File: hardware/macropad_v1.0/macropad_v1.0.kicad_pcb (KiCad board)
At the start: 2 copper layers, 61.9 x 76.2 mm, 50 parts, among them J1 USB_C_Receptacle_USB2.0_14P, SW1 SW_Push, SW2 Rotary Encoder, SW3 Rotary Encoder, U1 USBLC6-2SC6, U2 STM32F072C8T6, U3 XC6206PxxxMR

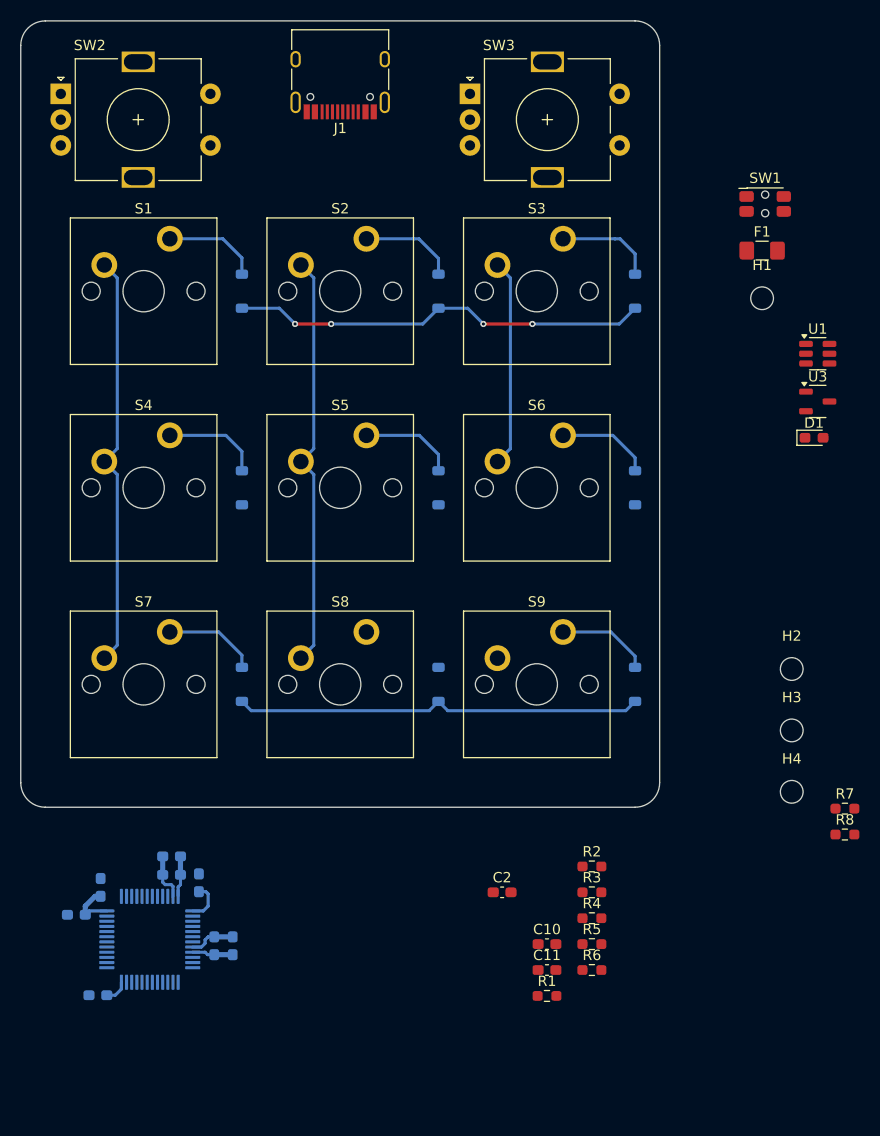
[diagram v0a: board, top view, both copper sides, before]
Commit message: finished routing decoupling caps & usb-c module
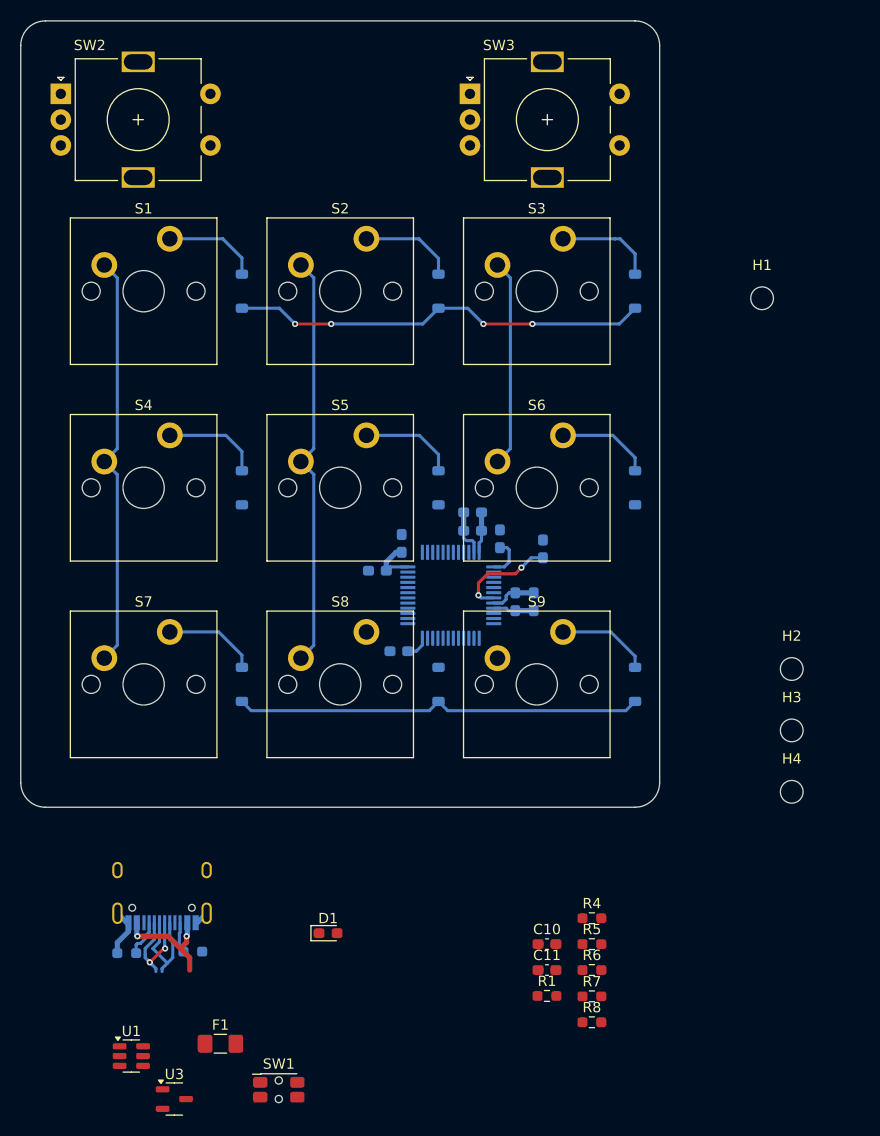
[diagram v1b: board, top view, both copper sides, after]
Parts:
- C2, J1, R2, R3: moved to B.Cu
- moved SW1 97.9 mm to (79.8, 125.0)
- moved U1 95.2 mm to (65.5, 121.7)
- moved F1 93.1 mm to (74.1, 120.6)
- moved U3 92.0 mm to (69.7, 125.9)
- moved J1 80.5 mm to (68.5, 104.8), turned to 0 degrees
- moved D1 67.2 mm to (84.6, 109.8)
- moved R2 45.9 mm to (65.0, 111.8), turned to 180 degrees
- moved C3 44.3 mm to (91.7, 72.1)
- moved C5 44.3 mm to (91.4, 82.5)
- moved C6 44.3 mm to (98.6, 70.8)
- moved C7 44.3 mm to (98.6, 69.1)
- moved C8 44.3 mm to (102.7, 77.7)
- moved C9 44.3 mm to (104.5, 77.7)
- moved U2 44.3 mm to (96.4, 77.1)
- moved C4 44.3 mm to (89.3, 74.7)
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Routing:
- net VBUS: track 0.00 -> 11.2 mm, vias 0 -> 2
- net ESD_D-: track 0.00 -> 10.1 mm, vias 0 -> 2
- net ESD_D+: track 0.00 -> 10.1 mm
- net /NRST: track 0.00 -> 10.0 mm, vias 0 -> 2
- net GND: track 9.12 -> 15.4 mm
- net Net-(J1-CC1): track 0.00 -> 3.64 mm
- net Net-(J1-CC2): track 0.00 -> 2.99 mm

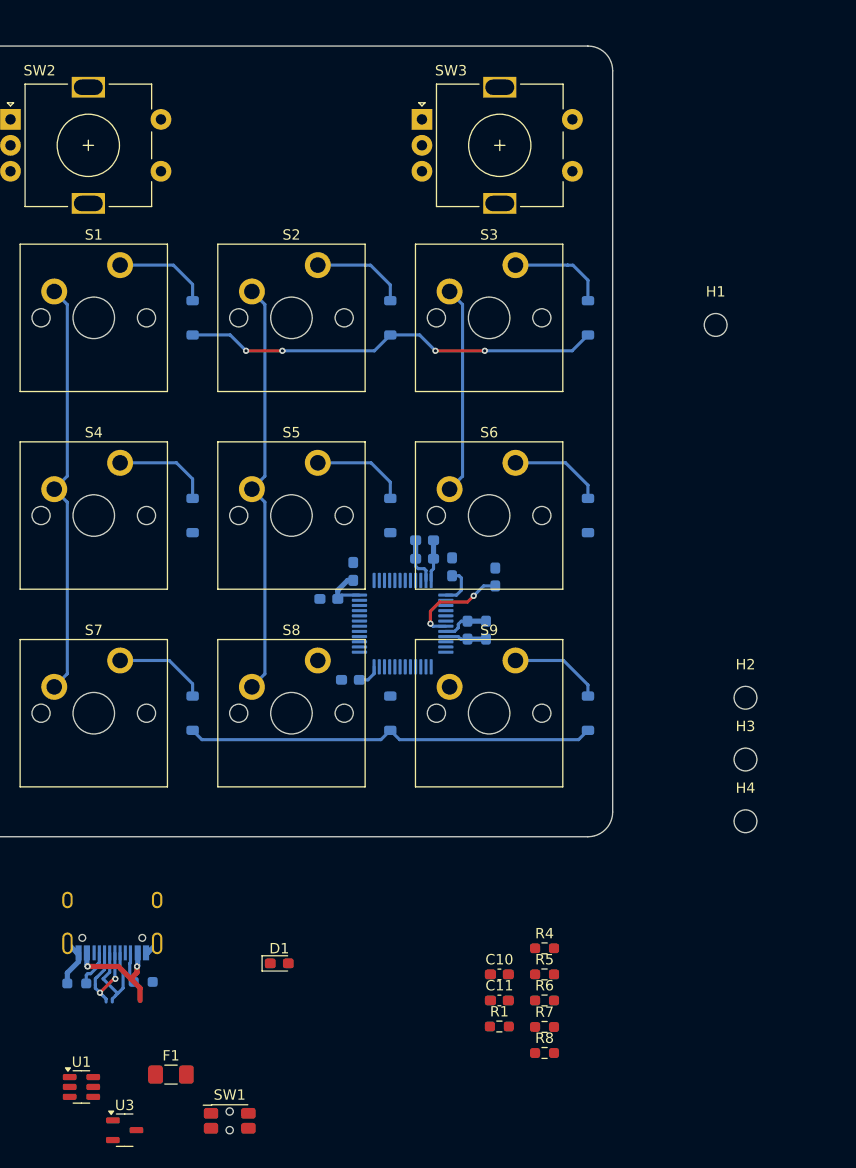
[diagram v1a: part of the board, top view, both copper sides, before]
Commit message: updated some 3d models, finished routing usb and esd protection
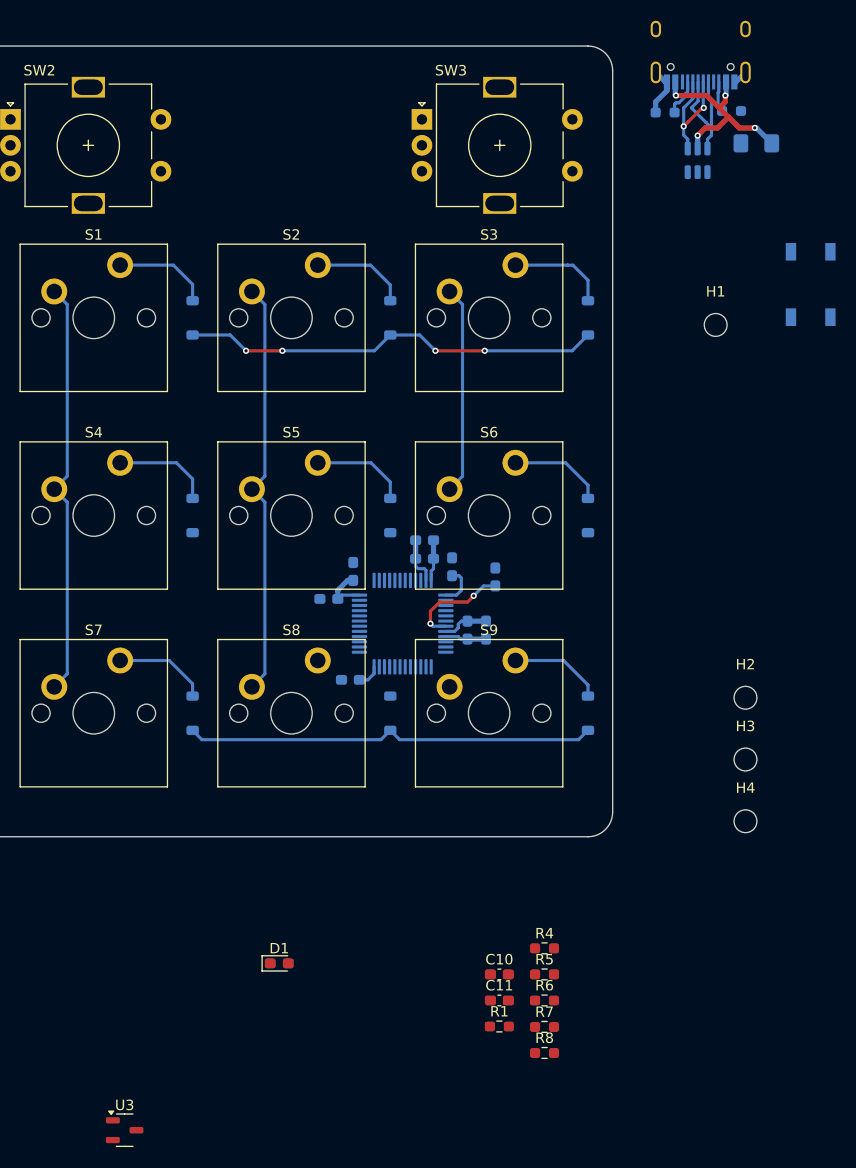
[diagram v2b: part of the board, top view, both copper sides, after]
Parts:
- F1, U1: moved to B.Cu
- SW1: footprint Button_Switch_SMD:SW_SPST_EVQP7C -> ScottoKeebs_Components:Button_TL3342; moved to B.Cu
- moved U1 107.2 mm to (124.9, 32.4), turned to 90 degrees
- moved F1 106.0 mm to (130.5, 30.8), turned to 180 degrees
- moved J1 101.3 mm to (125.2, 20.8)
- moved R2 101.3 mm to (121.7, 27.8)
- moved R3 101.3 mm to (128.1, 27.7)
- moved SW1 98.1 mm to (135.8, 44.4), turned to 90 degrees
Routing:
- net VBUS: track 11.2 -> 20.2 mm, vias 2 -> 4
- net ESD_D+: track 10.1 -> 12.2 mm
- net ESD_D-: track 10.1 -> 12.1 mm

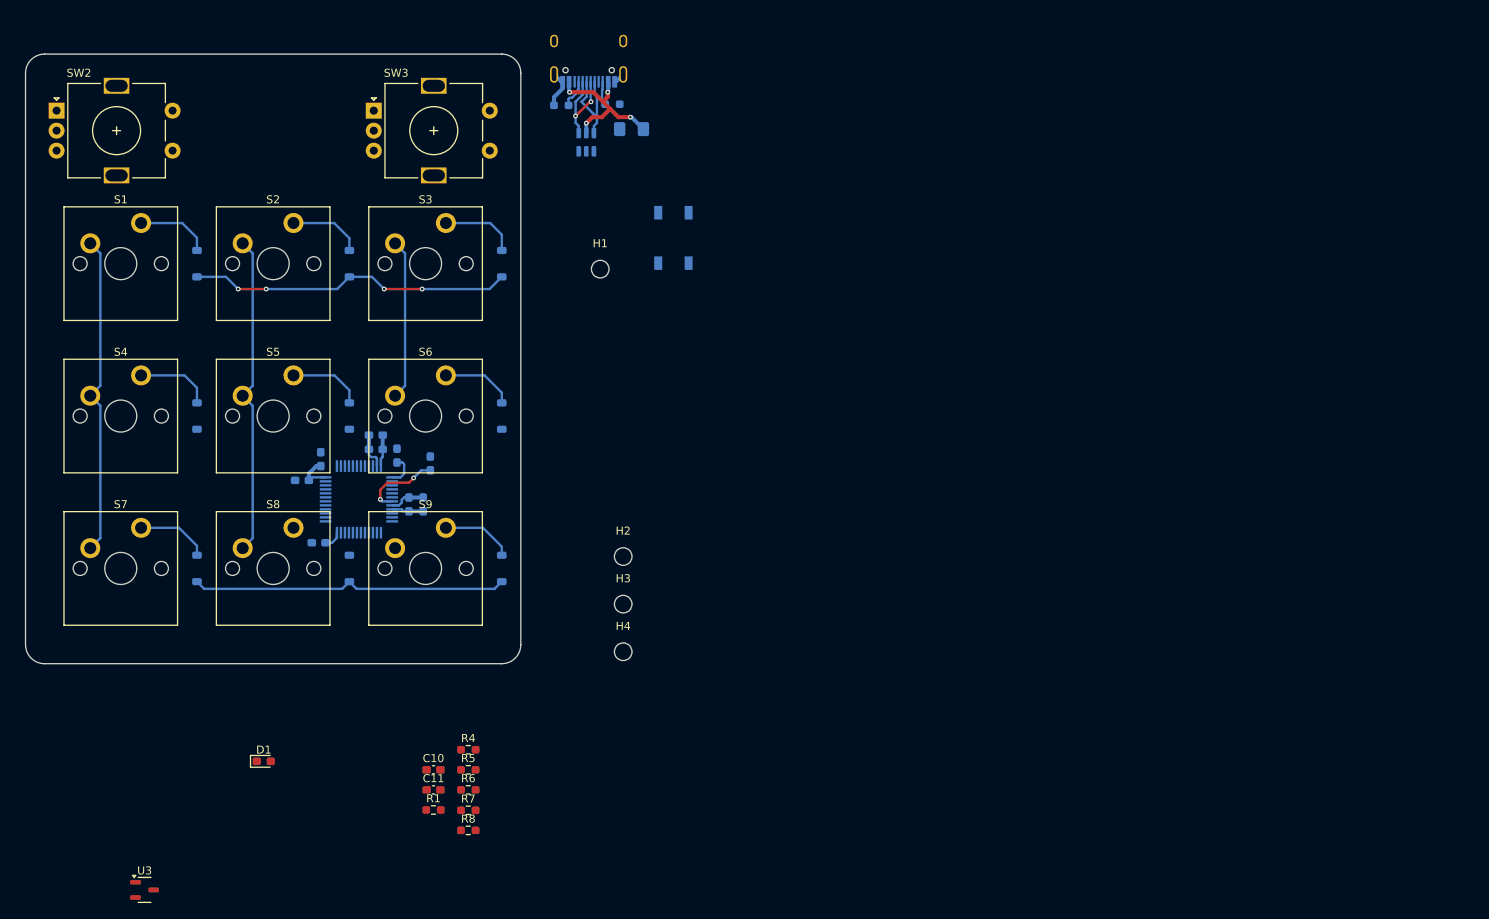
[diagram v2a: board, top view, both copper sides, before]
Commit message: finished routing everything except gnd and a few diodes
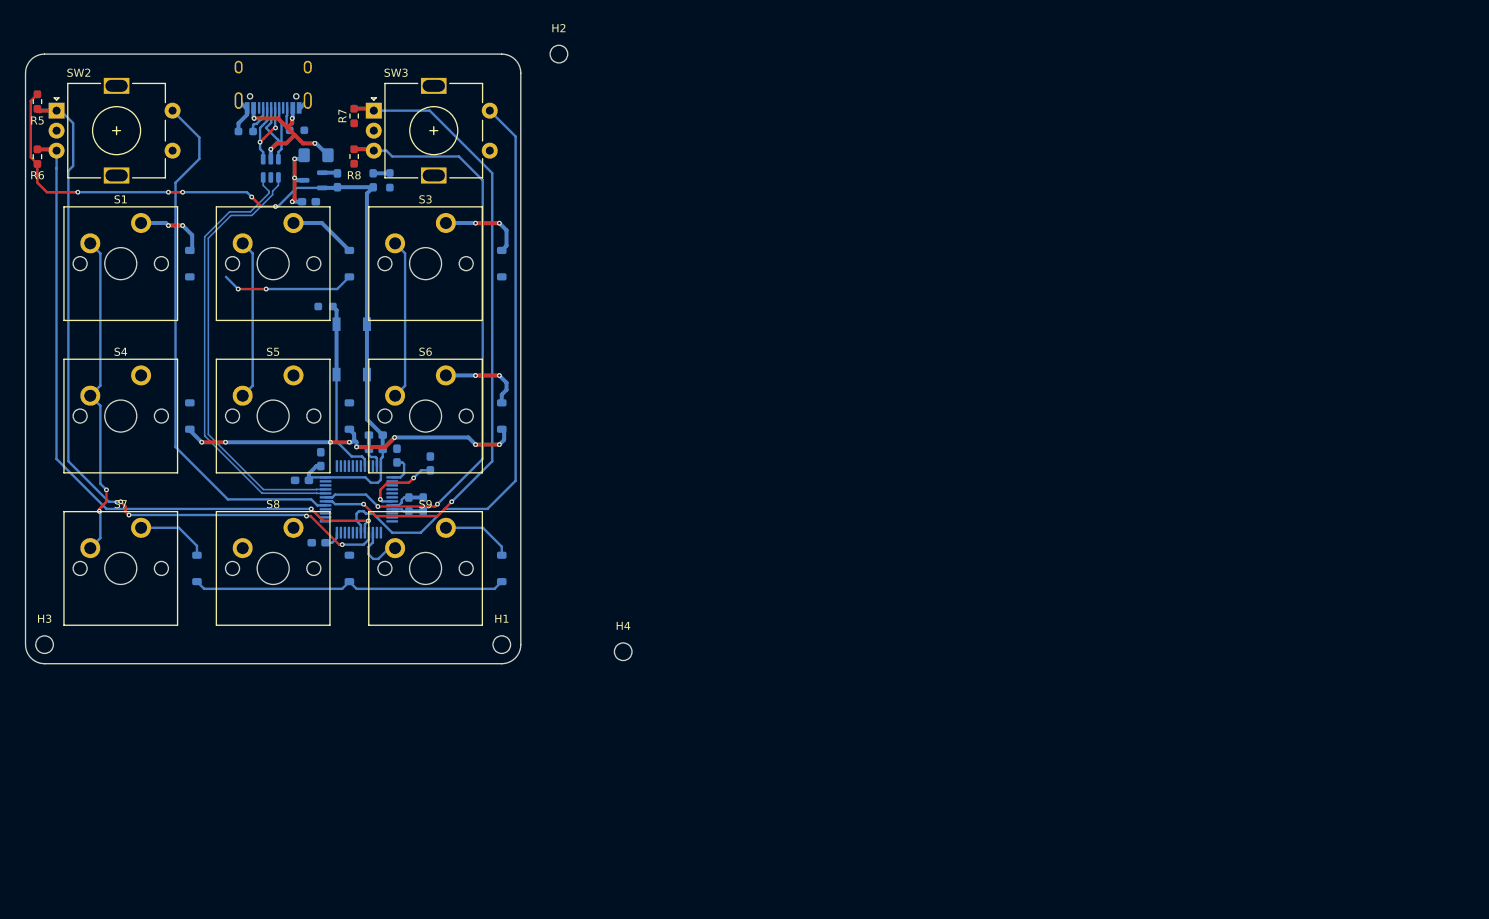
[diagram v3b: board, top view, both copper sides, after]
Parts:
- C10, C11, D1, R1, R4, U3: moved to B.Cu
- moved R5 99.4 mm to (56.3, 27.4), turned to -90 degrees
- moved R6 95.7 mm to (56.3, 34.2), turned to 90 degrees
- moved U3 91.2 mm to (90.7, 37.2), turned to 180 degrees
- moved R7 88.0 mm to (95.8, 29.2), turned to 90 degrees
- moved R8 85.4 mm to (95.8, 34.2), turned to 90 degrees
- moved C11 77.1 mm to (93.8, 37.2), turned to 90 degrees
- moved D1 73.9 mm to (98.2, 37.2), turned to -90 degrees
- moved C10 72.7 mm to (90.2, 39.9)
- moved H3 72.5 mm to (57.1, 95.2)
- moved R4 71.9 mm to (100.3, 37.2), turned to -90 degrees
- moved R1 64.4 mm to (92.3, 53.0), turned to 180 degrees
- moved H2 63.3 mm to (121.4, 21.4)
- moved H1 48.5 mm to (114.3, 95.2)
- moved SW1 42.6 mm to (95.5, 58.3)
- moved R2 39.6 mm to (82.3, 31.1)
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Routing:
- net VBAT: track 19.1 -> 116.2 mm, vias 0 -> 5
- net RENC_A1: track 0.00 -> 91.1 mm, vias 0 -> 4
- net RENC_B1: track 0.00 -> 84.9 mm, vias 0 -> 2
- net RENC_A2: track 0.00 -> 81.0 mm, vias 0 -> 2
- net RENC_B2: track 0.00 -> 75.4 mm, vias 0 -> 2
- net RENC_SW2: track 0.00 -> 74.0 mm
- net RENC_SW1: track 0.00 -> 66.4 mm
- net USB_D-: track 0.00 -> 55.6 mm
- net USB_D+: track 0.00 -> 54.8 mm
- net ROW_1: track 0.00 -> 45.0 mm, vias 0 -> 8
- net ROW_0: track 40.6 -> 16.7 mm, vias 4 -> 2
- net BOOT0: track 0.00 -> 22.4 mm
- net COL_1: track 40.2 -> 20.1 mm
- net Net-(D5-A): track 9.50 -> 0.00 mm
- net +5V: track 0.00 -> 9.40 mm, vias 0 -> 3
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
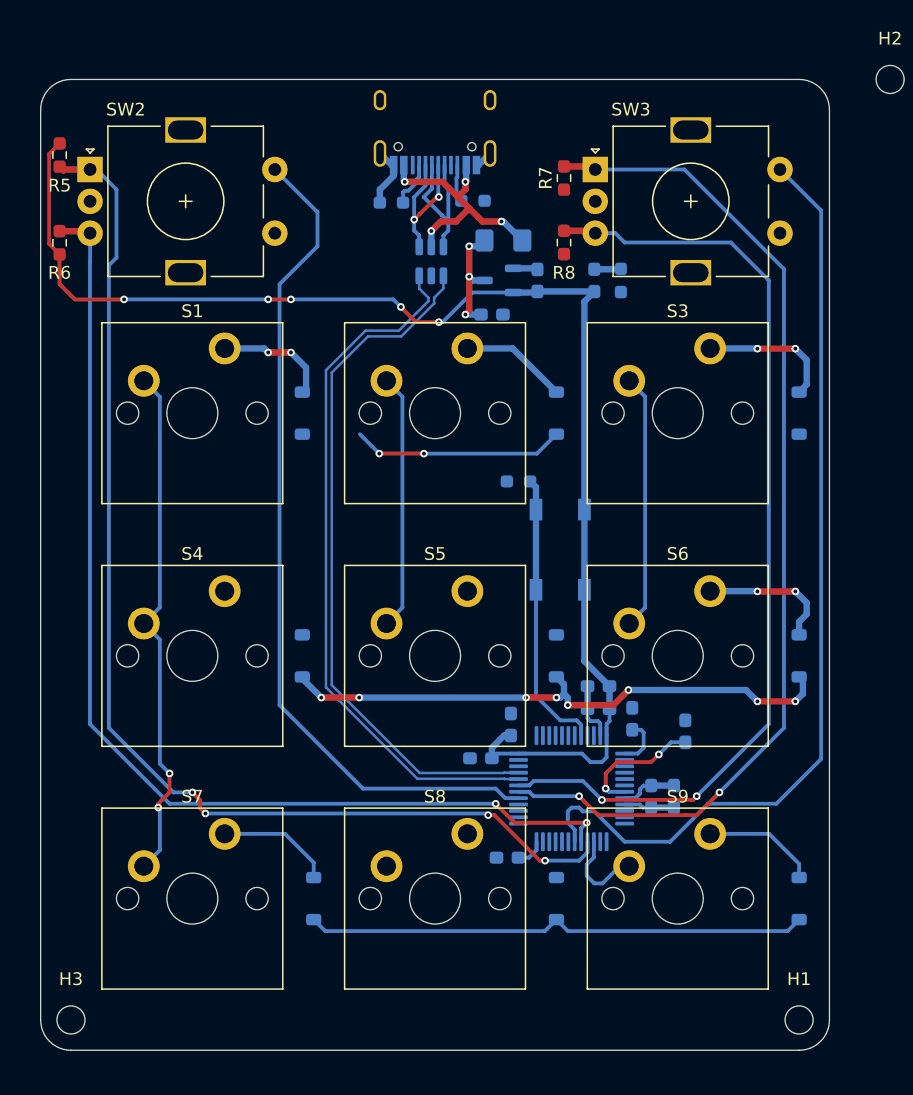
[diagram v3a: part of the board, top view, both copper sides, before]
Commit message: routed a bunch of stuff but realized all my vias were the wrong size so I still have to reroute oops
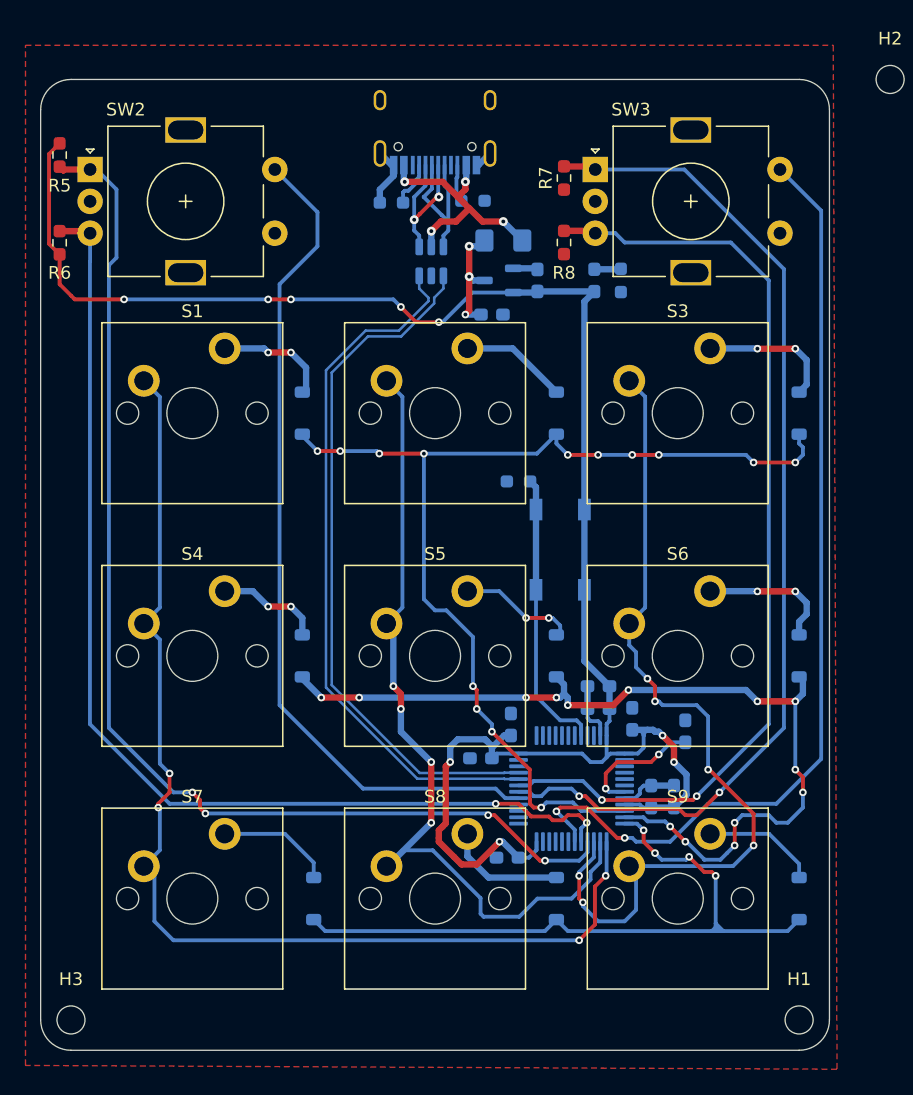
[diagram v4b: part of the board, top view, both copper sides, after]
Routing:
- net ROW_0: track 16.7 -> 83.4 mm, vias 2 -> 14
- net COL_0: track 40.9 -> 88.2 mm, vias 2 -> 4
- net COL_1: track 20.1 -> 66.0 mm, vias 0 -> 4
- net COL_2: track 27.2 -> 69.0 mm, vias 0 -> 6
- net VBAT: track 116.2 -> 148.6 mm, vias 5 -> 9
- net ROW_1: track 45.0 -> 72.2 mm, vias 8 -> 14
- net ROW_2: track 39.6 -> 55.2 mm, vias 0 -> 4
- net Net-(D9-A): track 0.00 -> 9.44 mm
- net Net-(D6-A): track 0.00 -> 9.25 mm, vias 0 -> 2
- net Net-(D5-A): track 0.00 -> 8.29 mm, vias 0 -> 2
- net RENC_SW2: track 74.0 -> 75.3 mm, vias 0 -> 2
- added copper zone on F.Cu, net GND
